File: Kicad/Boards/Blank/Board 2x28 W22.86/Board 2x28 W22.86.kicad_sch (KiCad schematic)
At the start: 4 parts, among them IC1 AP7365-33WG-7, J1 Board 2x24 W15.24mm

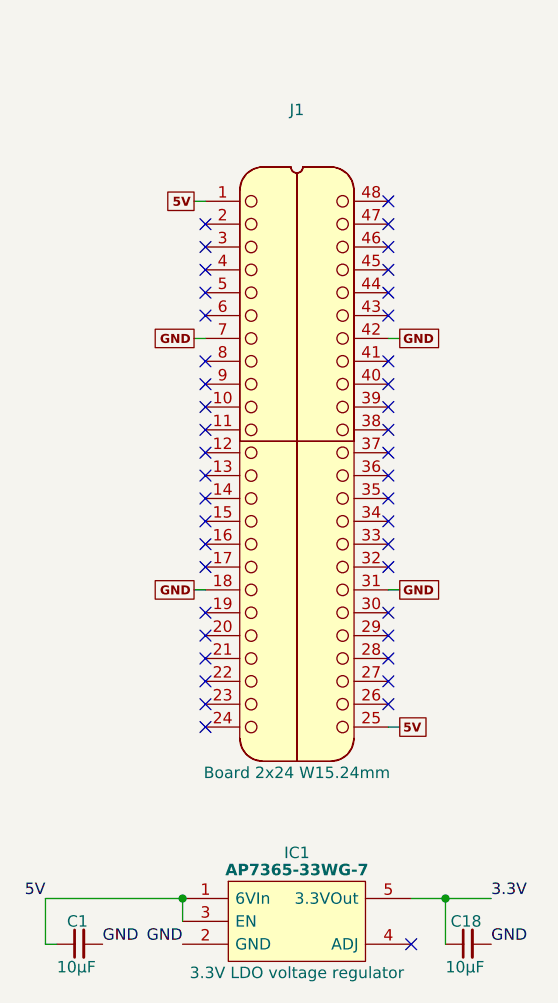
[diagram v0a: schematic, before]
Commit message: Added all blank board projects.
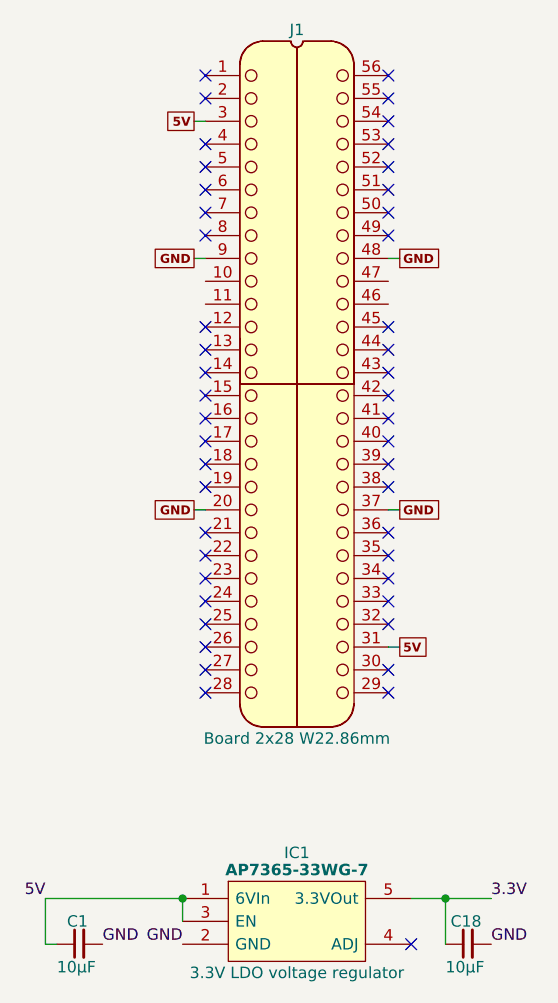
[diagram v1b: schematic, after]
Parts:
- J1: value Board 2x24 W15.24mm -> Board 2x28 W22.86mm; footprint SamacSys_Parts:DIP-48_Board_W15.24mm -> SamacSys_Parts:DIP-56_Board_W22.86mm; symbol HCP65:Board_02x24_W15.24mm -> HCP65:Board_02x28_W22.86mm
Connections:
- net 5V: now also J1.3, J1.31; no longer J1.1, J1.25
- net GND: now also J1.20, J1.37, J1.48, J1.9; no longer J1.18, J1.31, J1.42, J1.7
- no-connect marks 43 -> 47
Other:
- title: Board 2x24 W15.24mm -> Board 2x28 W22.86mm
